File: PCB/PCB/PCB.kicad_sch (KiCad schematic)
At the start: 6 parts, among them SW1 SW_Push, SW2 SW_Push, SW3 SW_Push, SW4 SW_Push, SW5 RotaryEncoder, U1 MOUDLE-SEEEDUINO-XIAO

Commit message: delete innecesary files and add new production files
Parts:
- removed SW5: RotaryEncoder, Rotary_Encoder:RotaryEncoder_Alps_EC11E_Vertical_H20mm, symbol Device:RotaryEncoder
- added SW5: RotaryEncoder_Switch, Rotary_Encoder:RotaryEncoder_Alps_EC11E-Switch_Vertical_H20mm, symbol Device:RotaryEncoder_Switch
- added U2: ER_OLEDM0.91_1x-I2C, Display:ER_OLEDM0.91_1x-I2C, symbol Display_Graphic:ER_OLEDM0.91_1x-I2C
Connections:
- net GND: now also SW1.1, U1.8 (PB09_A7_D7_RX), SW5.C, SW5.S2, U2.1 (GND)
- net at U1.12 (3V3): now also U2.2 (VCC)
- net at U1.2 (PA4_A1_D1): now also SW5.A
- net at U1.3 (PA10_A2_D2): now also SW5.B
- net at U1.4 (PA11_A3_D3): now also SW5.S1
- net at U1.5 (PA8_A4_D4_SDA): now also U2.4 (SDA)
- net at U1.6 (PA9_A5_D5_SCL): now also U2.3 (SCL)

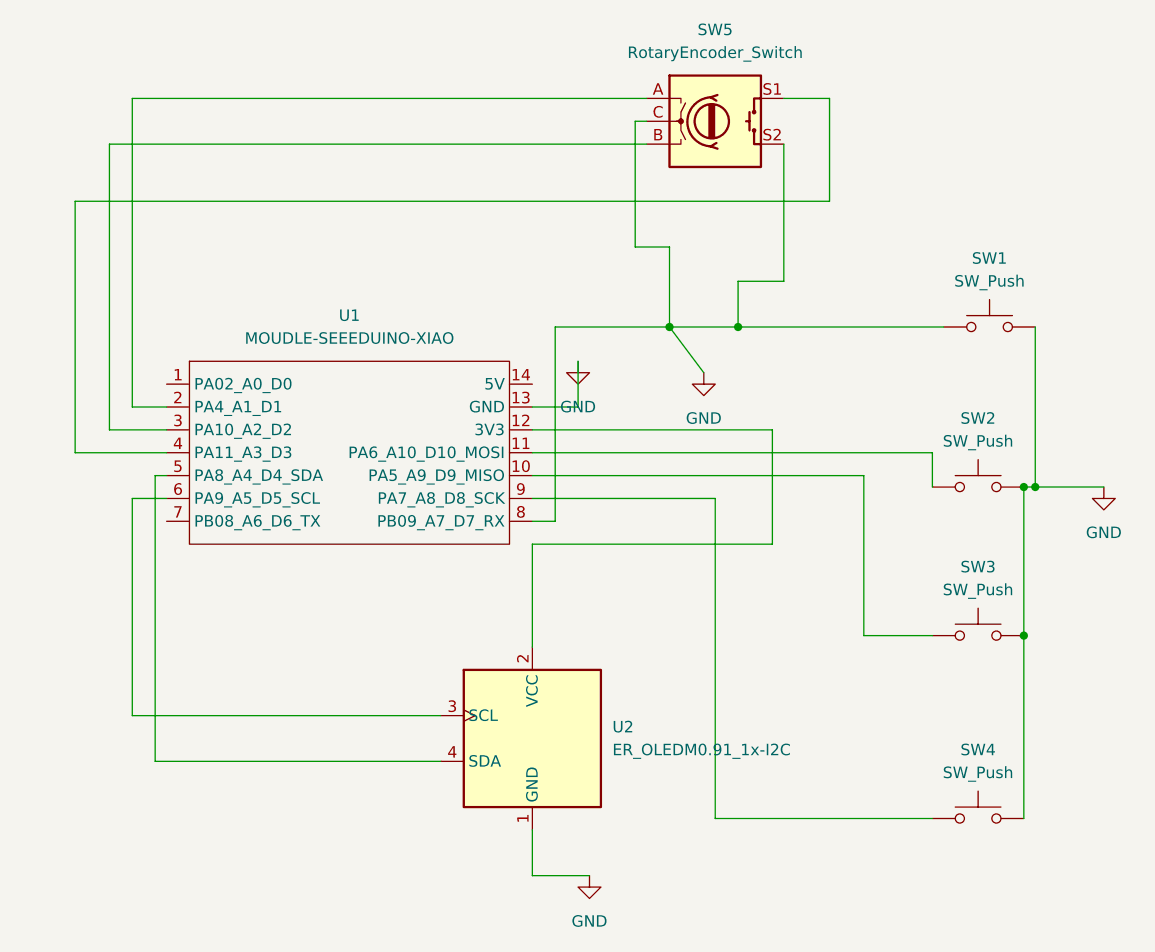
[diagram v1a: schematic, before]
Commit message: Update PCB adding resistors
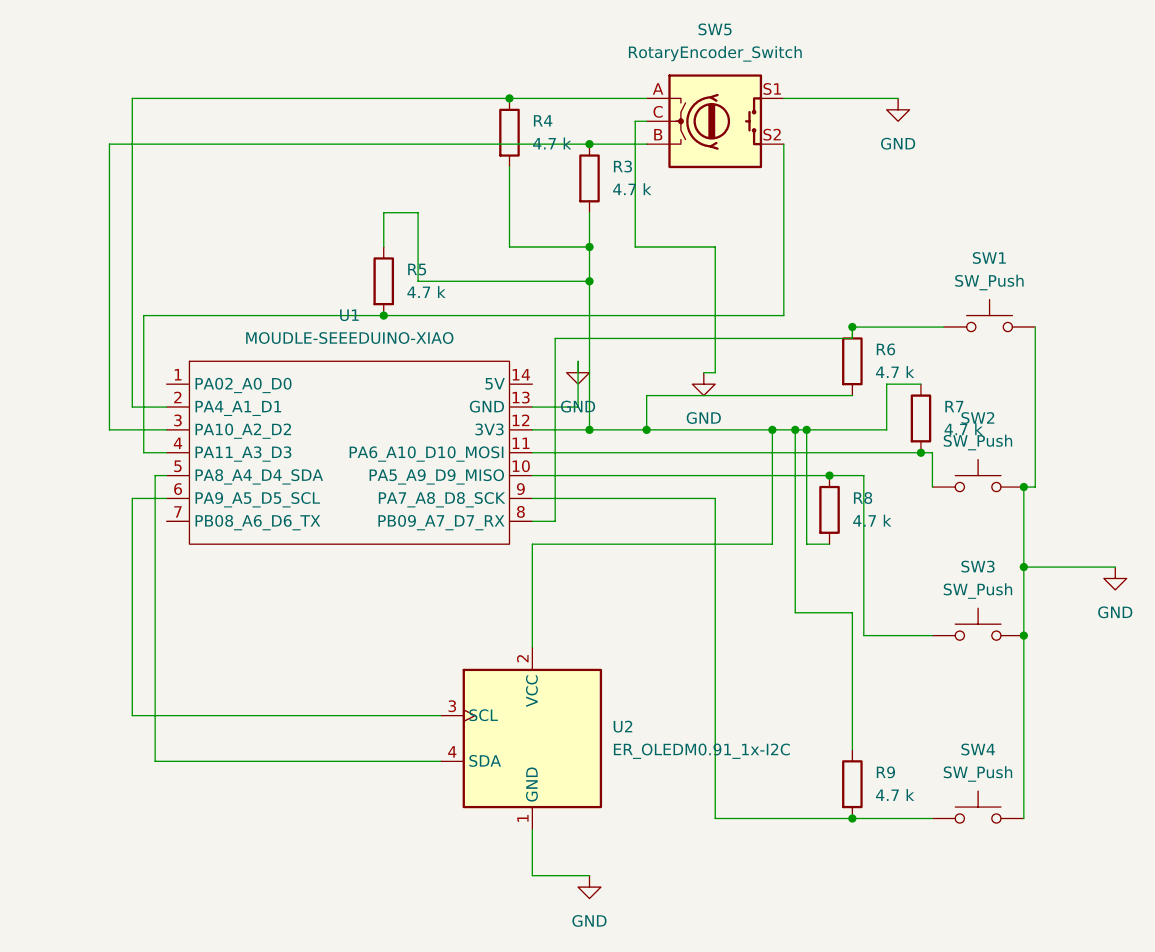
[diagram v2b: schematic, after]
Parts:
- added R3, R4, R5, R6, R7, R8, R9: 4.7 k, Resistor_THT:R_Axial_DIN0204_L3.6mm_D1.6mm_P1.90mm_Vertical, symbol Device:R
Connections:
- net GND: now also SW5.S1; no longer SW1.1, SW5.S2, U1.8 (PB09_A7_D7_RX)
- net at SW3.1, U1.10 (PA5_A9_D9_MISO): now also R8.1
- net at SW4.1, U1.9 (PA7_A8_D8_SCK): now also R9.2
- net at SW5.A, U1.2 (PA4_A1_D1): now also R4.1
- net at SW5.B, U1.3 (PA10_A2_D2): now also R3.1
- net at U1.4 (PA11_A3_D3): now also SW5.S2, R5.2; no longer SW5.S1
- net at SW2.1, U1.11 (PA6_A10_D10_MOSI): now also R7.2
- net at U1.12 (3V3), U2.2 (VCC): now also R3.2, R4.2, R5.1, R6.2, R7.1, R8.2, R9.1
- new net: R6.1, SW1.1, U1.8 (PB09_A7_D7_RX)

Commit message: Add files via upload
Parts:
- removed R3, R4, R5, R6, R7, R8, R9: 4.7 k, Resistor_THT:R_Axial_DIN0204_L3.6mm_D1.6mm_P1.90mm_Vertical, symbol Device:R
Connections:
- net GND: no longer SW5.S1
- net at SW5.B: now also U1.4 (PA11_A3_D3); no longer U1.3 (PA10_A2_D2)
- net at SW5.S2: now also U1.2 (PA4_A1_D1); no longer U1.4 (PA11_A3_D3)
- net at SW5.A: now also U1.1 (PA02_A0_D0); no longer U1.2 (PA4_A1_D1)
- new net: SW5.S1, U1.3 (PA10_A2_D2)
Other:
- moved on the sheet: SW5
